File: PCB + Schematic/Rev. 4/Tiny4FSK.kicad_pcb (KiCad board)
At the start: 4 copper layers, 24 x 69.5 mm, 72 parts, among them J1 SWD, J2 GPIO, J4 USB, J5 I2C, J6 Power Ext, J7 SPI, SW1 RST, SW2 Power Switch, U1 BME280, U2 ATGM336H, U3 SI4063, U4 ATSAMD21G18A-A, U5 1XZA032768AD19, U6 TPS61200DRC

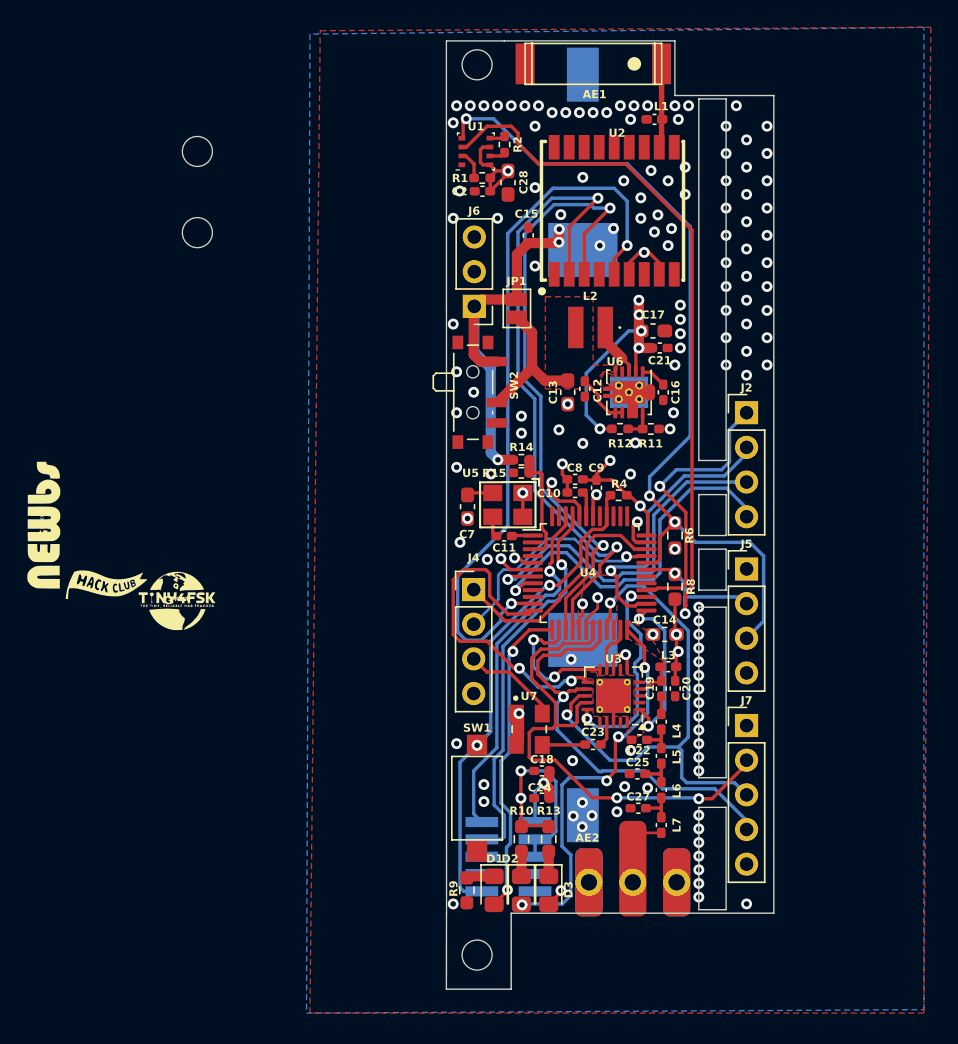
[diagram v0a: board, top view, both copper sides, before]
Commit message: USB, 3D models, Reference Designators
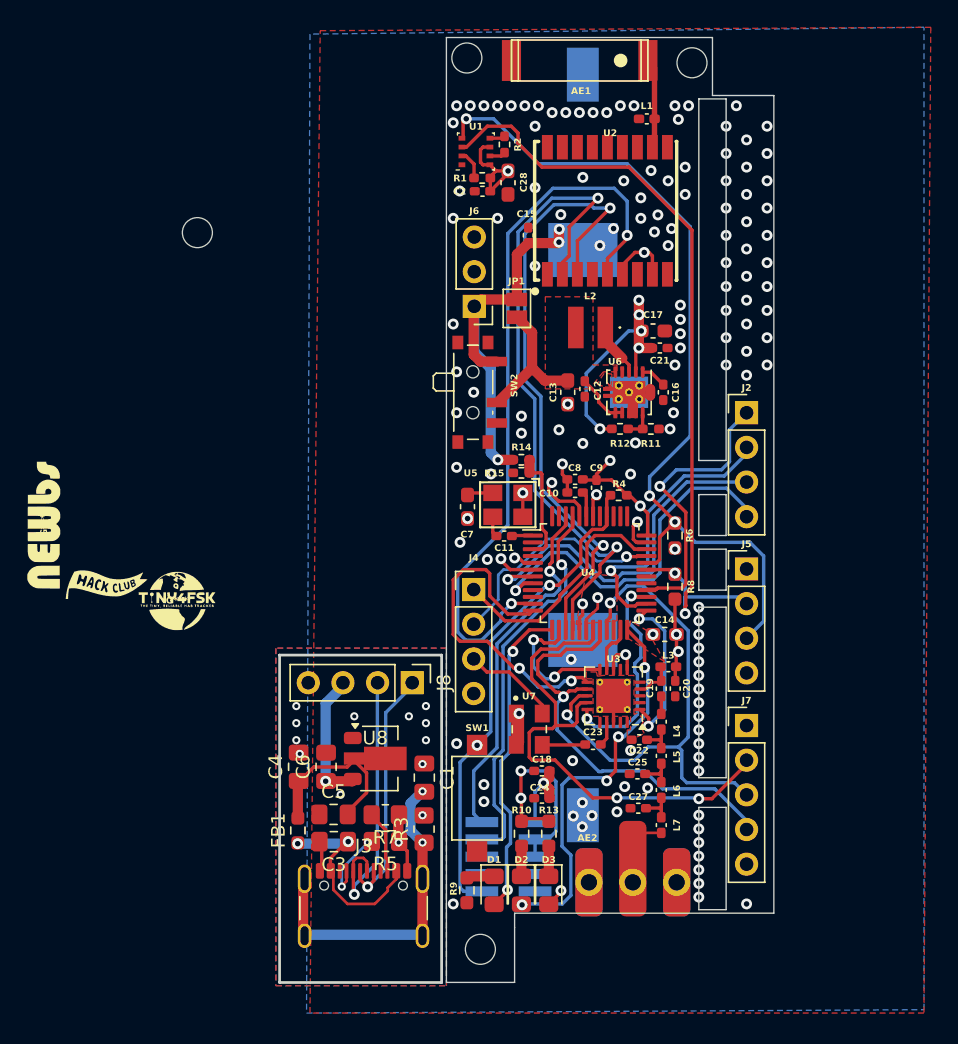
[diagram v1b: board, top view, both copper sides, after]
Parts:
- added C1: 4.5 nF, Capacitor_SMD:C_0805_2012Metric_Pad1.18x1.45mm_HandSolder, F.Cu at (138.6, 98.0)
- added C3: 100 nF, Capacitor_SMD:C_0805_2012Metric_Pad1.18x1.45mm_HandSolder, F.Cu at (132.0, 102.7)
- added C4: 100 nF, Capacitor_SMD:C_0805_2012Metric_Pad1.18x1.45mm_HandSolder, F.Cu at (129.4, 97.2)
- added C5: 1uF, Capacitor_SMD:C_0805_2012Metric_Pad1.18x1.45mm_HandSolder, F.Cu at (132.0, 100.7)
- added C6: 1uF, Capacitor_SMD:C_0805_2012Metric_Pad1.18x1.45mm_HandSolder, F.Cu at (131.4, 97.2)
- added FB1: BLM18AG121SN1D, Resistor_SMD:R_0603_1608Metric_Pad0.98x0.95mm_HandSolder, F.Cu at (129.4, 101.9)
- added J3: USBC, Connector_USB:USB_C_Receptacle_GCT_USB4105-xx-A_16P_TopMnt_Horizontal, F.Cu at (134.2, 108.5)
- added J8: USB, Connector_PinHeader_2.54mm:PinHeader_1x04_P2.54mm_Vertical, F.Cu at (137.7, 91.0)
- added R3: 1M, Resistor_SMD:R_0805_2012Metric_Pad1.20x1.40mm_HandSolder, F.Cu at (138.6, 101.8)
- added R5: 5k1, Resistor_SMD:R_0805_2012Metric_Pad1.20x1.40mm_HandSolder, F.Cu at (135.8, 102.7)
- added R7: 5k1, Resistor_SMD:R_0805_2012Metric_Pad1.20x1.40mm_HandSolder, F.Cu at (135.8, 100.7)
- added U8: Linear Step-Down, LDO:MCP1700, F.Cu at (135.0, 96.6)
- moved H2 36.8 mm to (158.2, 45.6)
- moved AE1 1.03 mm to (156.5, 45.3)
- moved H1 0.90 mm to (141.8, 45.2)
- moved L1 0.56 mm to (154.9, 49.7)
- moved U2 0.50 mm to (152.2, 56.5)
- moved H4 0.49 mm to (142.7, 110.6)
- moved R10 0.40 mm to (145.8, 102.1)
- moved R13 0.40 mm to (147.8, 102.1)
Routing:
- net Net-(J3-SHIELD): track 0.00 -> 23.9 mm, vias 0 -> 2
- net D-: track 17.1 -> 37.6 mm, vias 1 -> 2
- net D+: track 17.9 -> 37.1 mm, vias 0 -> 1
- net USB: track 0.00 -> 14.6 mm, vias 0 -> 2
- net LIN: track 0.00 -> 12.1 mm
- net LDO: track 0.00 -> 9.80 mm, vias 0 -> 1
- net Earth: track 40.4 -> 46.5 mm, vias 136 -> 147
- net Net-(J3-CC1): track 0.00 -> 5.90 mm, vias 0 -> 2
- net Net-(J3-CC2): track 0.00 -> 4.51 mm
- added copper zone on In2.Cu, net Earth
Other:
- board size 24 x 69.5 mm -> 36.2 x 69.3 mm

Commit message: FAB output, USB
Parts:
- C3, C4, C5, C6: footprint Capacitor_SMD:C_0805_2012Metric_Pad1.18x1.45mm_HandSolder -> Capacitor_SMD:C_0402_1005Metric_Pad0.74x0.62mm_HandSolder
- J8: value USB -> USB Breakout
- R3: footprint Resistor_SMD:R_0805_2012Metric_Pad1.20x1.40mm_HandSolder -> Resistor_SMD:R_0402_1005Metric_Pad0.72x0.64mm_HandSolder
- moved C1 4.76 mm to (138.4, 93.2)
- moved C3 4.76 mm to (131.7, 97.9)
- moved C4 4.76 mm to (129.2, 92.4)
- moved C5 4.76 mm to (131.7, 95.9)
- moved C6 4.76 mm to (131.2, 92.5)
- moved FB1 4.76 mm to (129.1, 97.1)
- moved J3 4.76 mm to (133.9, 103.8)
- moved R3 4.76 mm to (138.4, 97.0)
- moved R5 4.76 mm to (135.5, 97.9)
- moved R7 4.76 mm to (135.5, 96.0)
- moved U8 4.76 mm to (134.8, 91.8)
- moved J8 3.55 mm to (137.5, 87.5)
- moved C16 0.25 mm to (156.4, 69.8)
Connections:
- C6 pad 1: LDO -> +3.3V
- J8 pad 3: LDO -> +3.3V
- U8 pad 2: LDO -> +3.3V
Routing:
- net D-: track 37.6 -> 53.3 mm, vias 2 -> 3
- net D+: track 37.1 -> 50.7 mm
- net LDO: track 9.80 -> 0.00 mm, vias 1 -> 0
- net +3.3V: track 72.4 -> 81.1 mm, vias 20 -> 21
- net Earth: track 46.5 -> 49.8 mm, vias 147 -> 152
- net LIN: track 12.1 -> 13.8 mm
- net GPS_EN: track 54.4 -> 55.3 mm, vias 2 -> 4
- net Net-(J3-SHIELD): track 23.9 -> 24.4 mm
- net USB: track 14.6 -> 15.2 mm
- removed copper zone on In2.Cu, net Earth
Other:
- board size 36.2 x 69.3 mm -> 36.3 x 69.2 mm

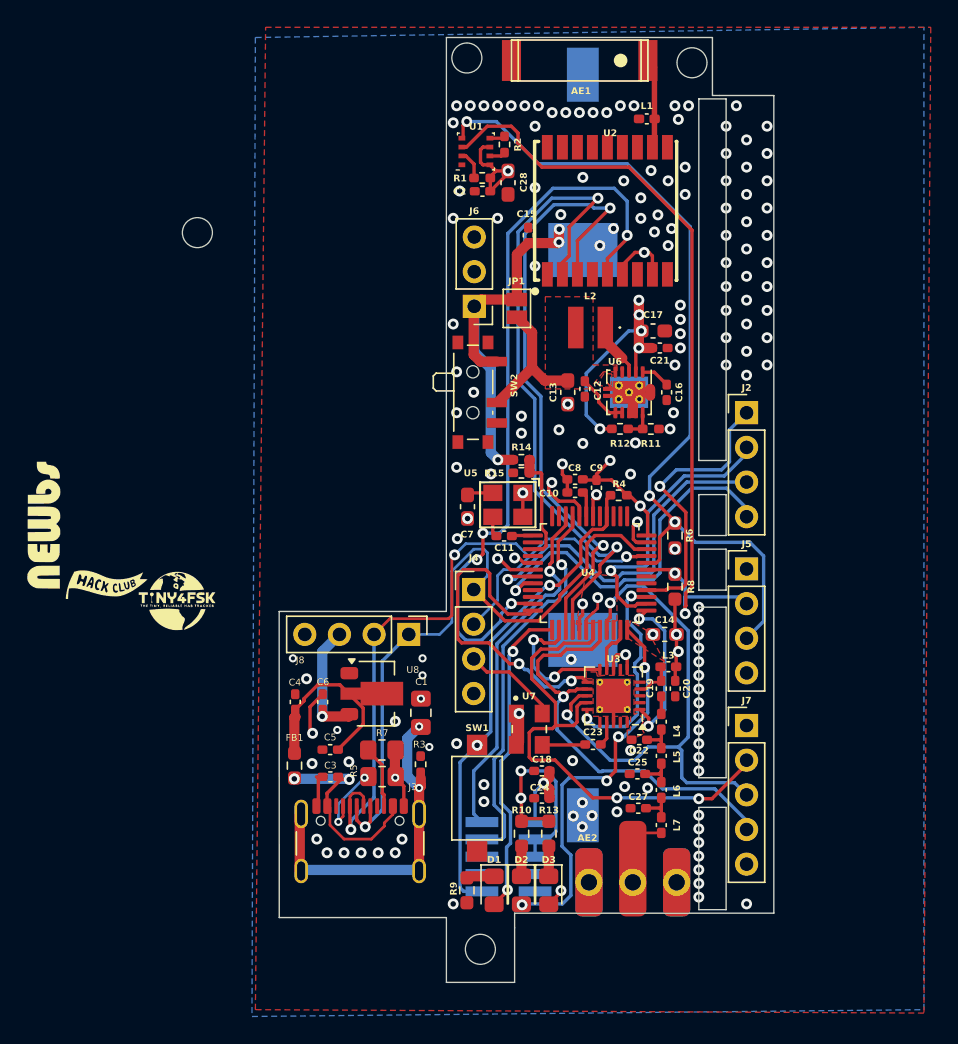
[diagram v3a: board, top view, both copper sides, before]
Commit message: Better Breakaway tabs, JLC export
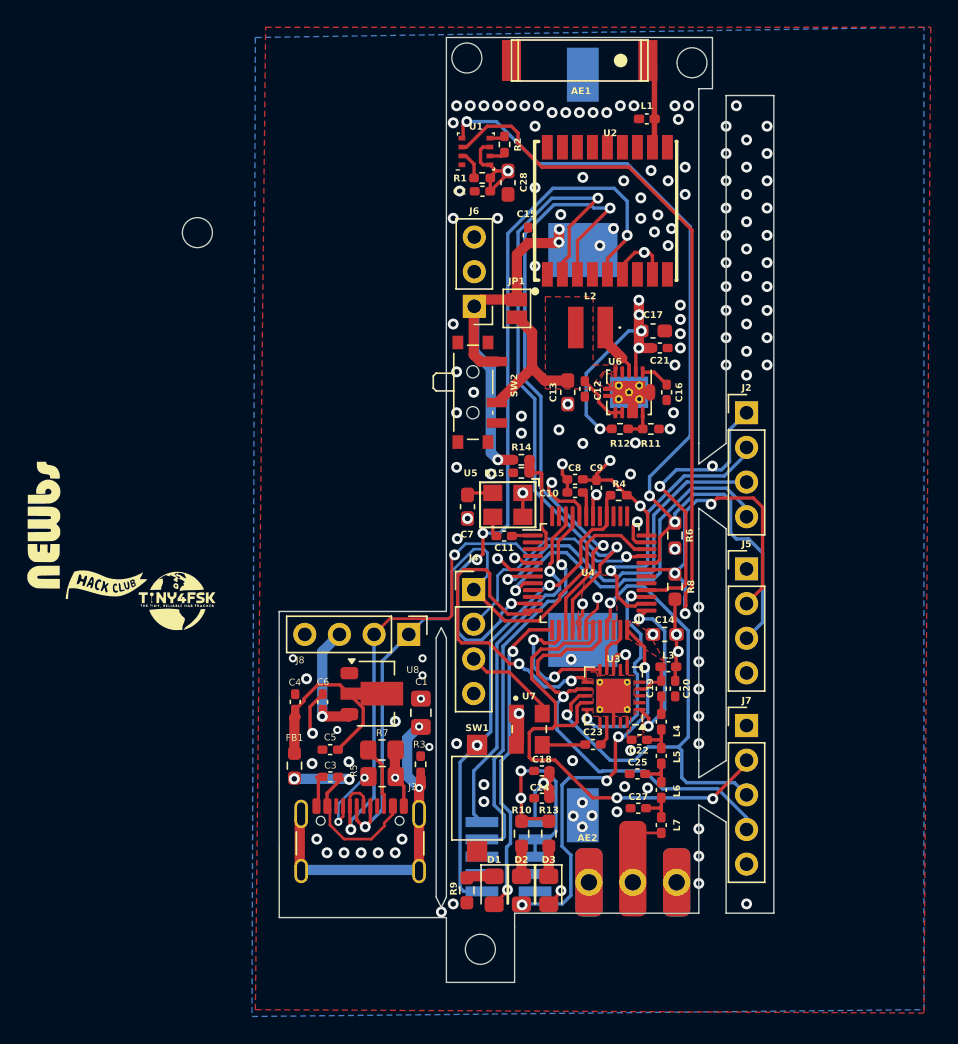
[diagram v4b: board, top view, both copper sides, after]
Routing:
- net SDA: track 60.8 -> 75.0 mm, vias 2 -> 3
- net SCL: track 63.0 -> 66.4 mm
- net D12: track 21.0 -> 21.2 mm, vias 1 -> 2
- net Earth: vias 152 -> 142
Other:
- outline, holes or cut-outs redrawn

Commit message: JLCPCB Centroid Fixes
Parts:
- moved AE1 6.52 mm to (150.0, 45.8), turned to 180 degrees
- moved J3 1.00 mm to (133.9, 102.8)
- moved U2 0.25 mm to (152.0, 56.5)
- turned U4 to -90 degrees
- turned U8 to 180 degrees

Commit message: Silkscreen, Pricing
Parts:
- added G***: LOGO, LOGO, B.Cu at (148.6, 67.9)
- added G***: LOGO, LOGO, B.Cu at (189.0, 73.9)
- added G***: LOGO, LOGO, B.Cu at (181.8, 89.8)
- added G***: LOGO, LOGO, B.Cu at (149.1, 83.0)
- added G***: LOGO, LOGO, B.Cu at (148.7, 80.2)
- added G***: LOGO, LOGO, B.Cu at (155.8, 102.8)
- added G***: LOGO, LOGO, B.Cu at (179.8, 95.5)
- moved G*** 72.0 mm to (182.2, 81.8)
- moved G*** 19.0 mm to (79.6, 65.8)
- moved FB1 1.27 mm to (127.9, 97.4)
- moved C1 1.27 mm to (137.1, 93.5)
- moved C3 1.27 mm to (130.5, 98.2)
- moved C4 1.27 mm to (127.9, 92.7)
- moved C5 1.27 mm to (130.5, 96.2)
- moved C6 1.27 mm to (129.9, 92.7)
- moved J3 1.27 mm to (132.7, 103.0)
- moved J8 1.27 mm to (136.2, 87.7)
- moved R3 1.27 mm to (137.1, 97.3)
- moved R5 1.27 mm to (134.3, 98.2)
- moved R7 1.27 mm to (134.3, 96.2)
- moved U8 1.27 mm to (133.5, 92.1)
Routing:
- net D-: track 53.3 -> 54.6 mm
- net D+: track 50.4 -> 51.8 mm
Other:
- board size 36.3 x 69.2 mm -> 37.5 x 69.2 mm
- board text added: "July 18, 2024"
- board text added: "Licensed under CERN-OHL-W-2.0"
- board text added: "Made by Max Kendall, W0MXX"
- board text added: "Made by Max W0MXX"
- board text added: "github.com/maxsrobotics/Tiny4FSK"

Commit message: JLCPCB export, Silkscreen
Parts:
- removed the G*** at (110.8, 79.5)
- removed the G*** at (189.0, 73.9)
- removed the G*** at (181.8, 89.8)
- removed the G*** at (120.5, 85.0)
- removed the G*** at (115.4, 83.8)
- removed the G*** at (79.6, 65.8)
- removed the G*** at (179.8, 95.5)
- removed the G*** at (182.2, 81.8)
- moved G*** 57.0 mm to (154.2, 45.8)
- moved G*** 37.1 mm to (145.8, 46.0)
- moved G*** 0.12 mm to (148.6, 80.2)
- renumbered C28 to C1, C9 to C10, C10 to C11, C7 to C12, C11 to C13, C19 to C15, C20 to C16, C4 to C17, C6 to C18, C1 to C19, C22 to C20, C23 to C21, C5 to C22, C18 to C23, C25 to C24, C3 to C25, C24 to C26, C15 to C3, C17 to C4, C21 to C5, C12 to C6, C13 to C7, C16 to C8, C8 to C9, J6 to J1, J5 to J3, J8 to J5, J7 to J6, J3 to J7, J1 to J8, R2 to R1, R7 to R10, R3 to R11, R5 to R12, R10 to R13, R13 to R14, R9 to R15, R1 to R2, R12 to R3, R11 to R4, R14 to R5, R15 to R6, R4 to R7, R6 to R8, R8 to R9, SW2 to SW1, SW1 to SW2, U6 to U3, U5 to U4, U4 to U5, U3 to U6, U8 to U7, U7 to U8
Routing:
- net Earth: vias 142 -> 132
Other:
- board text added: "JLCJLCJLCJLC"
- board text added: "Max W0MXX"
- board text added: "Rev. 2.0"
- board text added: "SNAP OFF TO REMOVE"
- board text added: "USB Breakout"
- board text removed: "Made by Max W0MXX"

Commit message: LNA Add-On, Silkscreen
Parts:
- added ?: , , B.Cu at (136.5, 49.5)
- added ?: , , B.Cu at (136.5, 59.5)
- added AE3: GPS1003, RF_Antenna_Extended:GPS1003, F.Cu at (136.3, 48.0)
- added C28: 100nF, Capacitor_SMD:C_0402_1005Metric_Pad0.74x0.62mm_HandSolder, F.Cu at (133.6, 55.2)
- added C29: 470 pF, Capacitor_SMD:C_0402_1005Metric_Pad0.74x0.62mm_HandSolder, F.Cu at (134.1, 53.5)
- added L8: 6.8 nH, Inductor_SMD:L_0402_1005Metric_Pad0.77x0.64mm_HandSolder, F.Cu at (133.1, 53.5)
- added U9: ~, Package_DFN_QFN:DFN-6-1EP_2x2mm_P0.65mm_EP1x1.6mm, F.Cu at (133.4, 50.5)
- moved H1 0.56 mm to (142.0, 45.8)
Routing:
- net Net-(U9-RFIN): track 0.00 -> 4.49 mm
- net Net-(AE3-A): track 0.00 -> 4.41 mm
- net RFOUT: track 0.00 -> 3.32 mm, vias 0 -> 1
- net Net-(C29-Pad1): track 0.00 -> 1.03 mm
- net Earth: track 49.8 -> 50.4 mm, vias 132 -> 134
- net +3.3V: track 81.2 -> 81.9 mm
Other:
- outline, holes or cut-outs redrawn
- board text added: "LNA Add-On"
